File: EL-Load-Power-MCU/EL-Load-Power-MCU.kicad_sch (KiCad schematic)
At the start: 68 parts, among them J1 Conn_01x02, J10 Power for serial interface, J11 Conn_02x08_Odd_Even, J2 Screw_Terminal_01x02, J3 Touchscreen, J4 JST-S6B-PH-SM4, J7 Conn_02x08_Odd_Even, J8 Conn_02x06_Odd_Even, T1 Wuerth_750316031, T2 Wuerth_750316031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

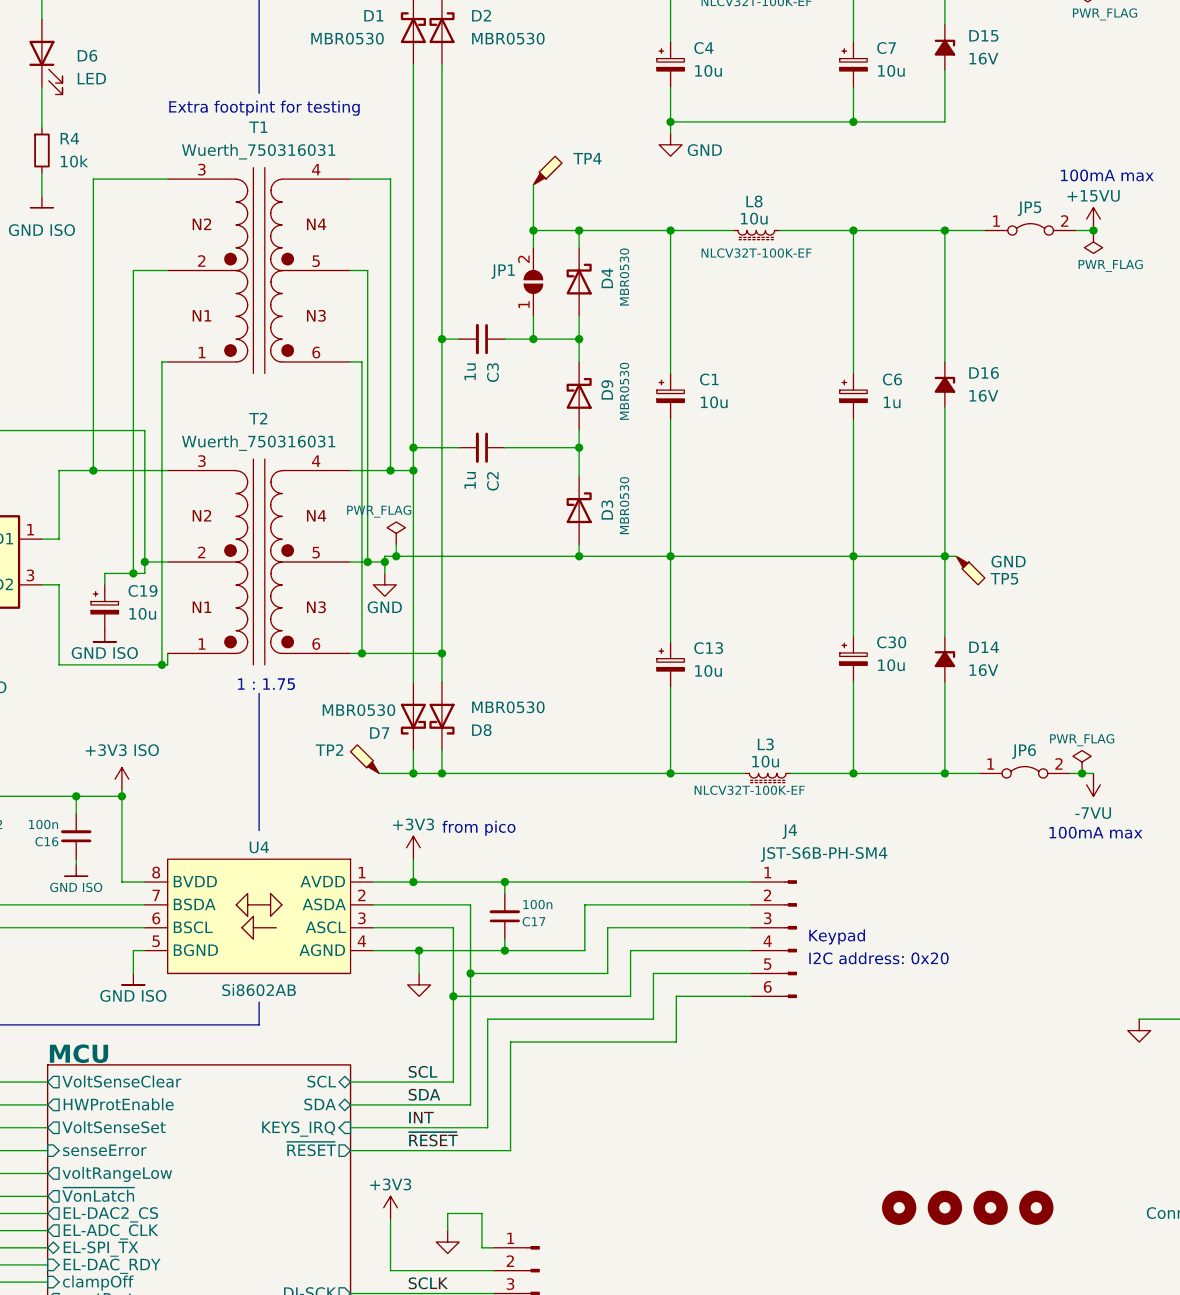
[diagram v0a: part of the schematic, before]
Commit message: Fixed Panel 1r1 and Power-MCU 2r2 versions
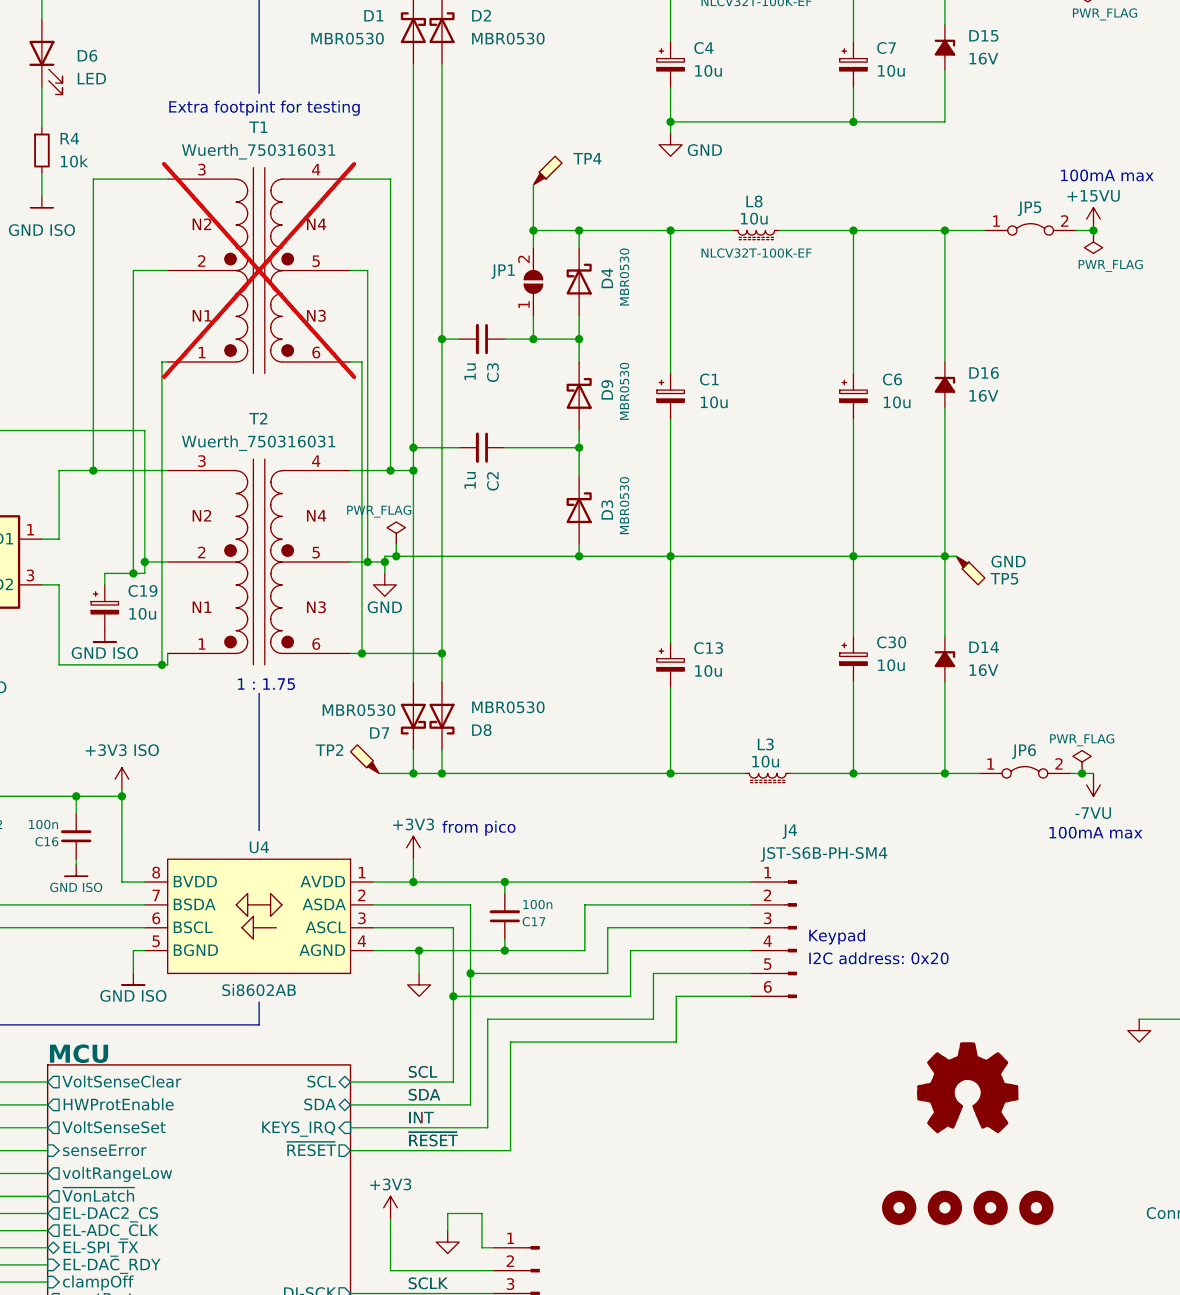
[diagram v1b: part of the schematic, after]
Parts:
- added PCB1: Logo_Open_Hardware_Small, symbol Graphic:Logo_Open_Hardware_Small
- C1, C13, C19, C30, C4, C7: Part_Name (none) -> C_47u_35V_Elec_6.3_20%
- C16, C17, C21: Part_Name (none) -> C_100.0nF_50V_0805_10%
- C18, C20, C22, C23, C24, C26: Part_Name (none) -> C_10.0uF_6V3_X7R_10%_0805
- C2, C3: Part_Name (none) -> C_1.0uF_0805_20%
- C6: value 1u -> 10u; Part_Name (none) -> C_47u_35V_Elec_6.3_20%
- D1, D2, D3, D4, D7, D8, D9: Part_Name (none) -> D_MBR0530T
- D12, D13, D6: Part_Name (none) -> D_LED_Groen_0805
- D14, D15, D16: Part_Name (none) -> D_Z_16V_miniMELF
- J1: Part_Name (none) -> H_Plug_2P_3.81MM_PCB_VERT
- J10: Part_Name (none) -> H_JST_XH_PCB_2P_VERT
- J11: Part_Name (none) -> H_IDC_2.54mm_Socket_THT_2x8pins
- J2: Part_Name (none) -> H_ScrewTerminal_2P_5.00MM_PCB_HORZ
- J3, J8, JP4, JP5, JP6, JP8: Consumable (none) -> 1; Part_Name (none) -> H_Male_1x40_vertical_THT
- J4: LCSC Part # C265405 -> (none); Optional (none) -> 1; Part_Name (none) -> H_JST_PH_THT_6P_HORZ
- J7: Part_Name (none) -> H_Female_2x8_SMD
- L1: Part_Name (none) -> LC_2000uH_0.6A_0905
- L2, L8: Part_Name (none) -> L_10uH_480mohm_450mA_
- L3: Part_Name (none) -> L_10uH_480mohm_450mA_; Type NLCV32T-100K-EF -> (none)
- R12, R13: Part_Name (none) -> R_3.0kΩ_0805_1%
- R14, R18, R4: Part_Name (none) -> R_10.0kΩ_0805_1%
- T1: now not fitted; now left out of the parts list
- T2: Part_Name (none) -> T_1:1:1.75:1.75_185uH_SMD
- U2: Part_Name (none) -> U_SN6505BDBVT_SOT-23-6
- U4: Part_Name (none) -> U_SI8602AB-B-IS
- U5, U9: Part_Name (none) -> U_AMS1117-3.3
- U7: Part_Name (none) -> U_ AZ1117CH-5.0TRG1

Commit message: BOM fixes/updates.
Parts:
- J4: Part_Name H_JST_PH_THT_6P_HORZ -> H_JST_PH_SMD_6P_HORZ
- J7: Consumable (none) -> 1; Part_Name H_Female_2x8_SMD -> H_Male_1x40_vertical_THT
- U7: Part_Name U_ AZ1117CH-5.0TRG1 -> U_AZ1117CH-5.0TRG1
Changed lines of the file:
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@@
       (effects (font (size 1.27 1.27)))
     )
-    (property "Part_Name" "H_Female_2x8_SMD" (at 74.295 181.61 0)
-      (effects (font (size 1.27 1.27)) hide)
-    )
-    (property "Consumable" "" (at 74.295 181.61 0)
+    (property "Part_Name" "H_Male_1x40_vertical_THT " (at 74.295 181.61 0)
+      (effects (font (size 1.27 1.27)) hide)
+    )
+    (property "Consumable" "1" (at 74.295 181.61 0)
       (effects (font (size 1.27 1.27)) hide)
     )
@@
       (effects (font (size 1.27 1.27)))
     )
-    (property "Part_Name" "H_JST_PH_THT_6P_HORZ" (at 175.895 128.27 0)
+    (property "Part_Name" "H_JST_PH_SMD_6P_HORZ" (at 175.895 128.27 0)
       (effects (font (size 1.27 1.27)) hide)
     )
@@
       (effects (font (size 1.27 1.27)) hide)
     )
-    (property "Part_Name" "U_ AZ1117CH-5.0TRG1 " (at 259.715 88.9 0)
-      (effects (font (size 1.27 1.27)) hide)
-    )
+    (property "Part_Name" "U_AZ1117CH-5.0TRG1 " (at 259.715 88.9 0)
+      (effects (font (size 1.27 1.27)) hide)
+    )

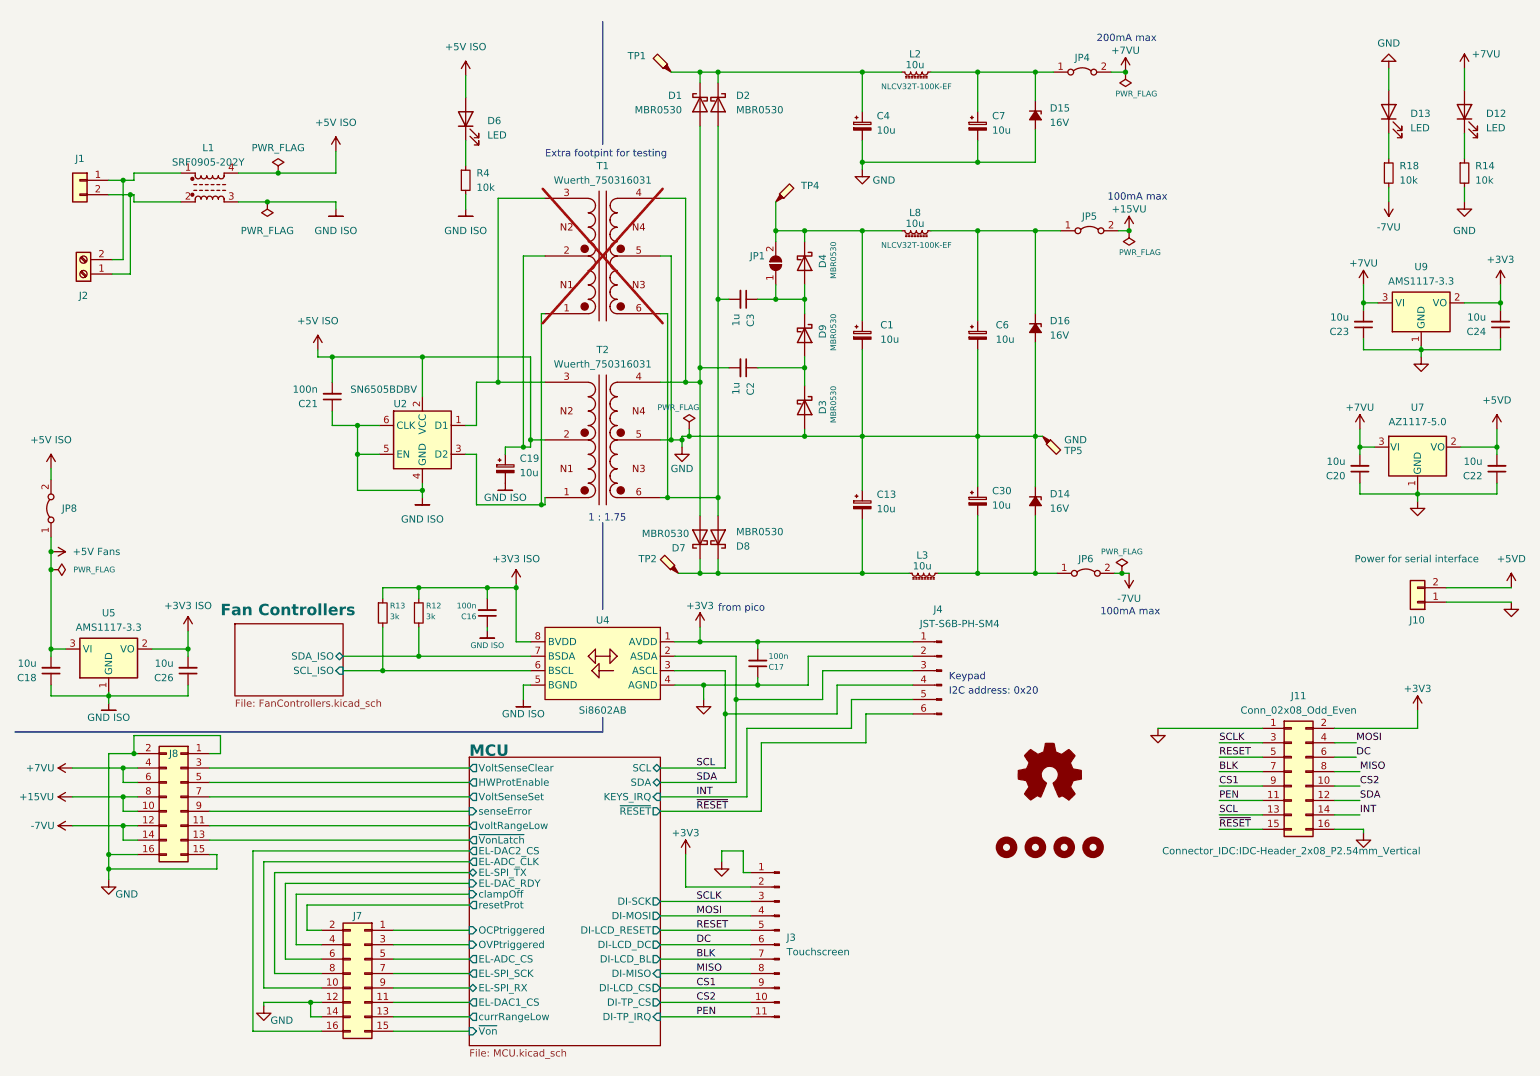
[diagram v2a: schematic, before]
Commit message: Fixes to Power-MCU board.
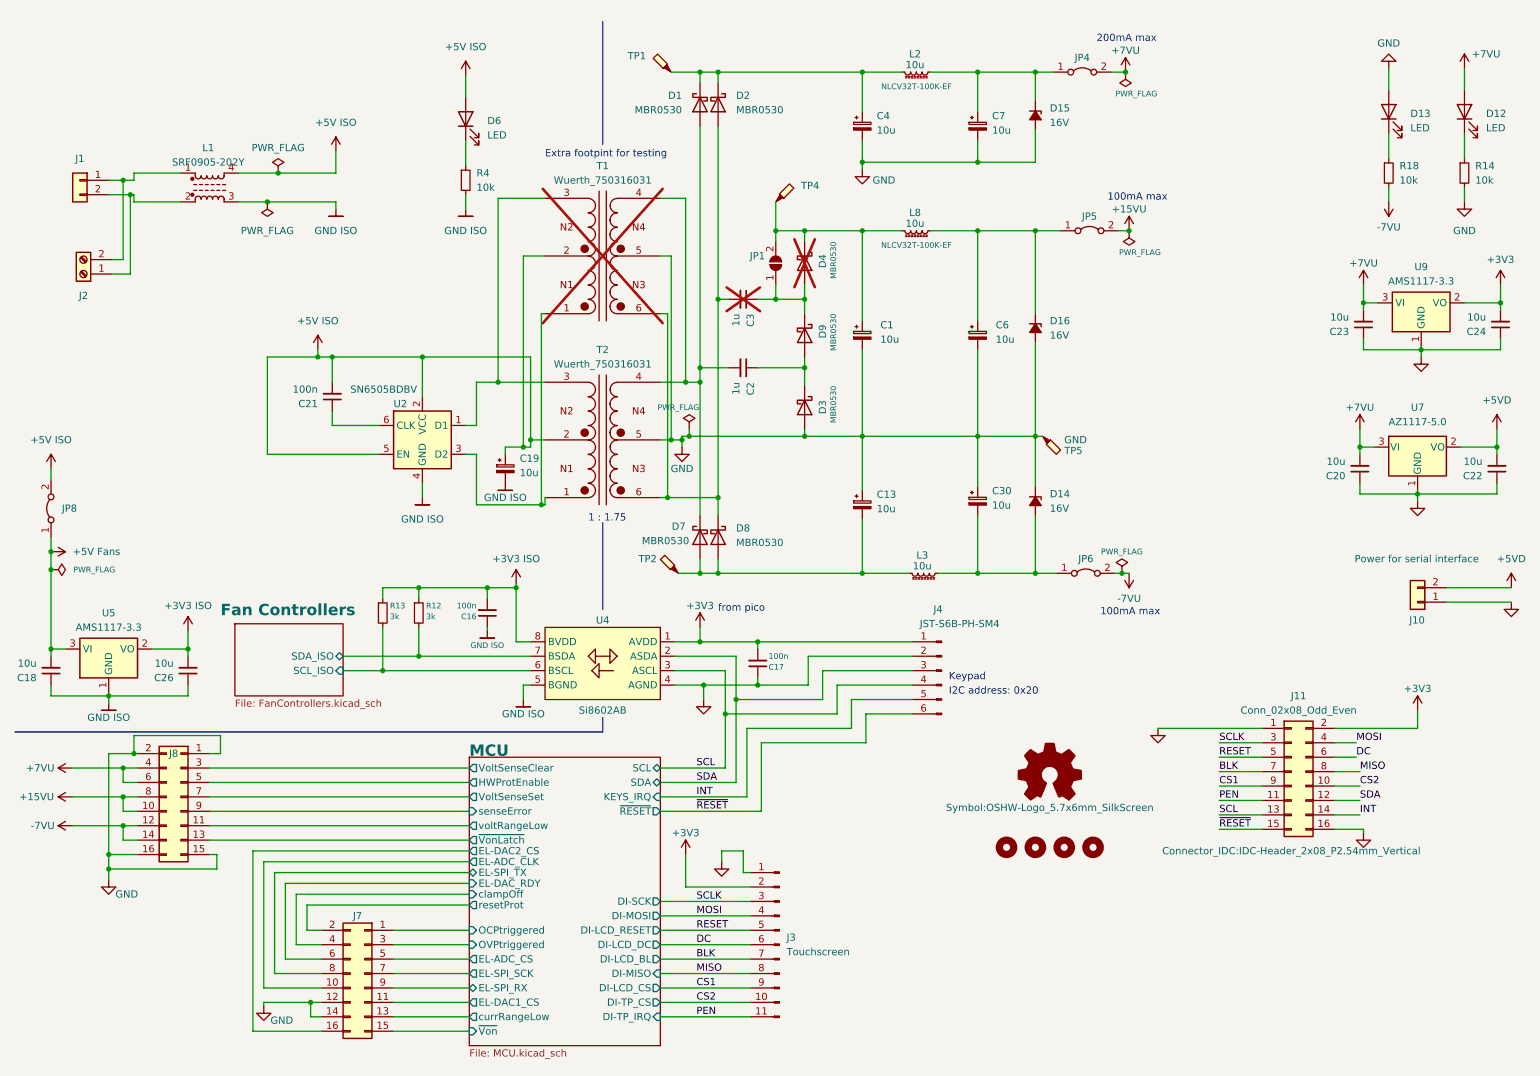
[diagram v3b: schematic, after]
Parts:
- C3, D4: now not fitted; now left out of the parts list
- PCB1: footprint (none) -> Symbol:OSHW-Logo_5.7x6mm_SilkScreen
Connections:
- net +5V_ISO: now also U2.5 (EN)
- net GND_ISO: no longer C21.1, U2.5 (EN), U2.6 (CLK)
- net at C2.2, D1.2 (A), T1.4 (N4-B)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: now also D7.1 (K); no longer D7.2 (A)
- net at C3.2, D2.2 (A), T1.6 (N3-A)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: now also D8.1 (K); no longer D8.2 (A)
- net at C13.2, L3.2, TP2.1: now also D7.2 (A), D8.2 (A); no longer D7.1 (K), D8.1 (K)
- new net: C21.1, U2.6 (CLK)
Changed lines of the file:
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@@
   (title_block
     (title "EL-Load-Power-MCU")
-    (date "2023-12-26")
+    (date "2024-02-04")
     (rev "${VERSION}r${PCBVERSION}")
   )
   (junction (at 19.05 124.46) (diameter 0) (color 0 0 0 0)
   )
+  (junction (at 66.04 73.025) (diameter 0) (color 0 0 0 0)
+  )
   (junction (at 259.715 97.155) (diameter 0) (color 0 0 0 0)
   )
@@
   (junction (at 260.35 71.755) (diameter 0) (color 0 0 0 0)
   )
-  (junction (at 73.025 90.17) (diameter 0) (color 0 0 0 0)
-  )
   (junction (at 146.685 50.8) (diameter 0) (color 0 0 0 0)
   )
@@
   (junction (at 136.525 62.865) (diameter 0) (color 0 0 0 0)
   )
-  (junction (at 84.455 96.52) (diameter 0) (color 0 0 0 0)
-  )
   (junction (at 97.79 77.47) (diameter 0) (color 0 0 0 0)
   )
@@
   (junction (at 127.635 97.79) (diameter 0) (color 0 0 0 0)
   )
-  (junction (at 73.025 85.09) (diameter 0) (color 0 0 0 0)
-  )
   (junction (at 128.27 87.63) (diameter 0) (color 0 0 0 0)
   )
@@
     (stroke (width 0) (type default))
   )
-  (wire (pts (xy 73.025 90.17) (xy 76.835 90.17))
+  (wire (pts (xy 57.15 90.17) (xy 76.835 90.17))
     (stroke (width 0) (type default))
   )
@@
     (stroke (width 0) (type default))
   )
-  (wire (pts (xy 68.58 85.09) (xy 73.025 85.09))
+  (wire (pts (xy 68.58 85.09) (xy 76.835 85.09))
     (stroke (width 0) (type default))
   )
@@
     (stroke (width 0) (type default))
   )
-  (wire (pts (xy 84.455 96.52) (xy 84.455 97.79))
+  (wire (pts (xy 84.455 95.25) (xy 84.455 97.79))
     (stroke (width 0) (type default))
   )
@@
     (stroke (width 0) (type default))
   )
-  (wire (pts (xy 84.455 95.25) (xy 84.455 96.52))
-    (stroke (width 0) (type default))
-  )
   (wire (pts (xy 141.605 138.43) (xy 160.02 138.43))
     (stroke (width 0) (type default))
@@
     (stroke (width 0) (type default))
   )
-  (wire (pts (xy 73.025 96.52) (xy 84.455 96.52))
-    (stroke (width 0) (type default))
-  )
   (wire (pts (xy 68.58 73.025) (xy 68.58 77.47))
     (stroke (width 0) (type default))
@@
     (stroke (width 0) (type default))
   )
-  (wire (pts (xy 73.025 90.17) (xy 73.025 96.52))
-    (stroke (width 0) (type default))
-  )
   (wire (pts (xy 103.505 87.63) (xy 106.045 87.63))
     (stroke (width 0) (type default))
@@
     (stroke (width 0) (type default))
   )
+  (wire (pts (xy 66.04 73.025) (xy 57.15 73.025))
+    (stroke (width 0) (type default))
+  )
   (wire (pts (xy 133.35 74.93) (xy 138.43 74.93))
     (stroke (width 0) (type default))
@@
     (stroke (width 0) (type default))
   )
-  (wire (pts (xy 76.835 85.09) (xy 73.025 85.09))
-    (stroke (width 0) (type default))
-  )
   (wire (pts (xy 151.765 85.725) (xy 151.765 86.995))
     (stroke (width 0) (type default))
@@
     (stroke (width 0) (type default))
   )
+  (wire (pts (xy 57.15 73.025) (xy 57.15 90.17))
+    (stroke (width 0) (type default))
+  )
   (wire (pts (xy 207.01 50.8) (xy 208.915 50.8))
     (stroke (width 0) (type default))
@@
     (stroke (width 0) (type default))
   )
-  (wire (pts (xy 73.025 85.09) (xy 73.025 90.17))
-    (stroke (width 0) (type default))
-  )
   (wire (pts (xy 66.04 73.025) (xy 68.58 73.025))
     (stroke (width 0) (type default))
@@
     )
   )
-  (symbol (lib_id "Diode:MBR0530") (at 133.35 104.775 90) (unit 1)
+  (symbol (lib_id "Diode:MBR0530") (at 133.35 104.775 90) (mirror x) (unit 1)
     (in_bom yes) (on_board yes) (dnp no)
-    (property "Reference" "D7" (at 130.81 106.68 90)
+    (property "Reference" "D7" (at 130.81 102.87 90)
       (effects (font (size 1.27 1.27)) (justify left))
     )
-    (property "Value" "MBR0530" (at 131.445 104.14 90)
+    (property "Value" "MBR0530" (at 131.445 105.41 90)
       (effects (font (size 1.27 1.27)) (justify left))
     )
@@
   )
   (symbol (lib_id "Device:C_Small") (at 140.97 62.865 270) (mirror x) (unit 1)
-    (in_bom yes) (on_board yes) (dnp no)
+    (in_bom no) (on_board no) (dnp yes)
     (property "Reference" "C3" (at 142.2337 65.405 0)
       (effects (font (size 1.27 1.27)) (justify right))
@@
     )
   )
-  (symbol (lib_id "Diode:MBR0530") (at 136.525 104.775 270) (mirror x) (unit 1)
+  (symbol (lib_id "Diode:MBR0530") (at 136.525 104.775 270) (unit 1)
     (in_bom yes) (on_board yes) (dnp no)
-    (property "Reference" "D8" (at 139.7 106.3625 90)
+    (property "Reference" "D8" (at 139.7 103.1875 90)
       (effects (font (size 1.27 1.27)) (justify left))
     )
-    (property "Value" "MBR0530" (at 139.7 103.8225 90)
+    (property "Value" "MBR0530" (at 139.7 105.7275 90)
       (effects (font (size 1.27 1.27)) (justify left))
     )
@@
   )
   (symbol (lib_id "Graphic:Logo_Open_Hardware_Small") (at 194.945 146.685 0) (unit 1)
-    (in_bom yes) (on_board no) (dnp no)
+    (in_bom yes) (on_board yes) (dnp no)
     (property "Reference" "PCB1" (at 194.945 139.7 0)
       (effects (font (size 1.27 1.27)) hide)
@@
       (effects (font (size 1.27 1.27)) hide)
     )
-    (property "Footprint" "" (at 194.945 146.685 0)
-      (effects (font (size 1.27 1.27)) hide)
+    (property "Footprint" "Symbol:OSHW-Logo_5.7x6mm_SilkScreen" (at 194.945 152.4 0)
+      (effects (font (size 1.27 1.27)))
     )
     (property "Datasheet" "~" (at 194.945 146.685 0)
@@
       (effects (font (size 1.27 1.27)) hide)
     )
+    (property "MPN" "" (at 194.945 146.685 0)
+      (effects (font (size 1.27 1.27)))
+    )
     (instances
       (project "EL-Load-Power-MCU"
@@
   )
   (symbol (lib_id "Diode:MBR0530") (at 151.765 56.515 270) (unit 1)
-    (in_bom yes) (on_board yes) (dnp no)
+    (in_bom no) (on_board no) (dnp yes)
     (property "Reference" "D4" (at 154.94 54.9275 0)
       (effects (font (size 1.27 1.27)) (justify left))
